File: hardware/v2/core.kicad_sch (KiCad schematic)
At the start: 15 parts, among them J201 USB4105-GF-A, J202 SM04B-SRSS-TB, SW201 EVQ-P7A01P, SW202 EVQ-P7A01P, U201 TCA9555RTWR, U202 ESP32-C3-WROOM-02

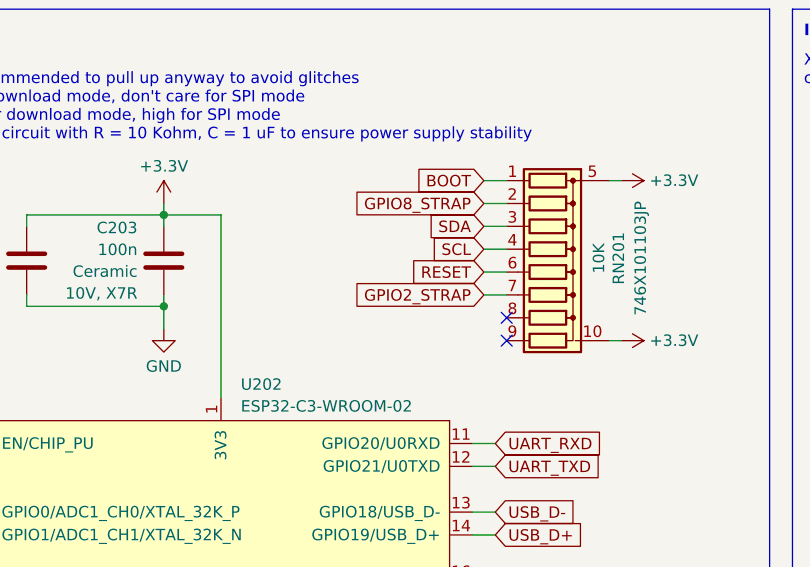
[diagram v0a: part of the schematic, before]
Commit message: Complete draft of the v2 PCB
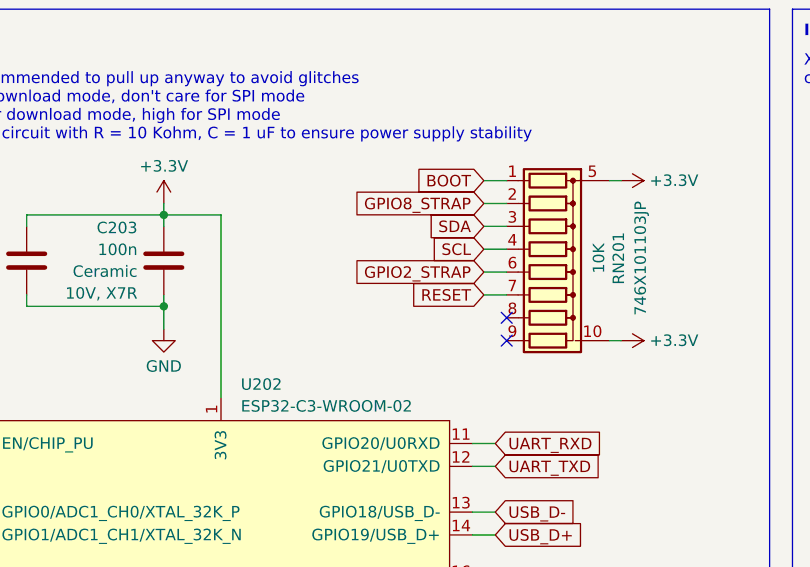
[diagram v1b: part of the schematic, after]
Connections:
- net GPIO2_STRAP: now also RN201.6 (R5); no longer RN201.7 (R6)
- net RESET: now also RN201.7 (R6); no longer RN201.6 (R5)

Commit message: Prepare Minuet v2 for fabrication.
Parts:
- R201, R202: Rating (none) -> 1%
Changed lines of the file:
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@@
+			)
+		)
+		(property "Rating" "1%"
+			(at 264.16 35.56 90)
+			(effects
+				(font
+					(size 1.27 1.27)
+				)
 			)
 		)
@@
 			)
 		)
+		(property "Rating" "1%"
+			(at 264.16 40.64 90)
+			(effects
+				(font
+					(size 1.27 1.27)
+				)
+			)
+		)
